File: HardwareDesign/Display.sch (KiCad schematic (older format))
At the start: 30 parts, among them J601 Conn_01x12, U601 Upduino_3.0, U602 IDT7201, U603 74LVC245, U604 74LVC245

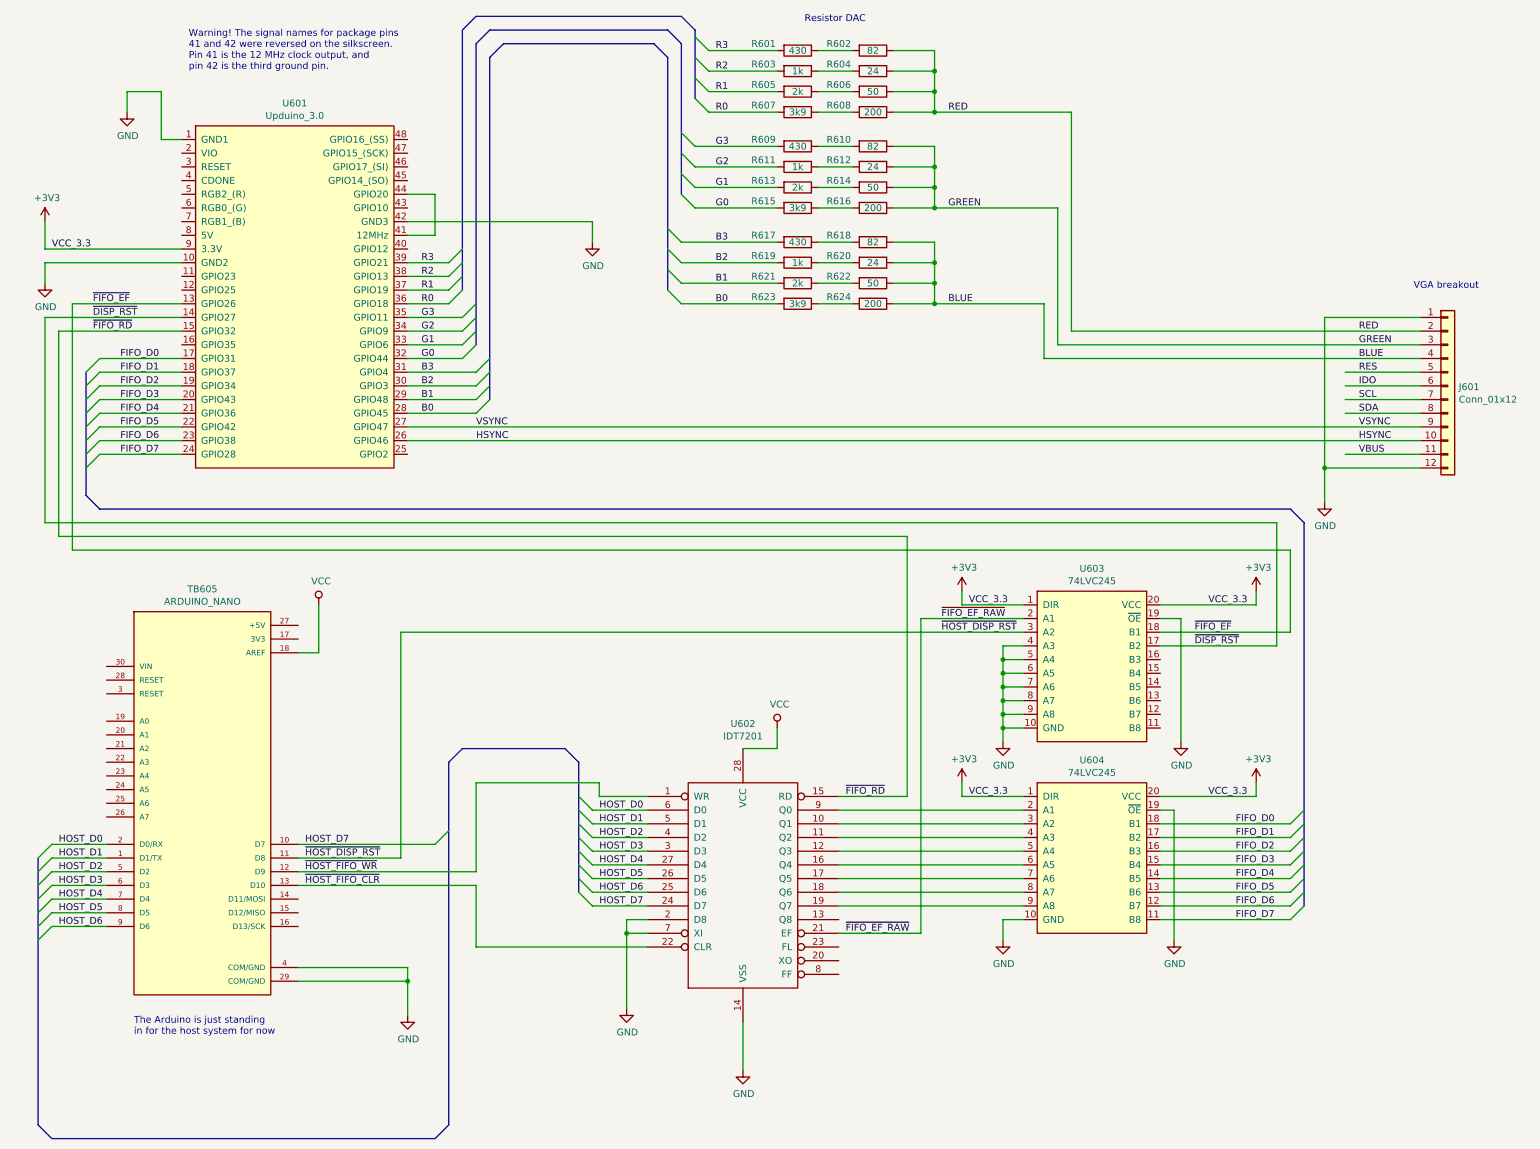
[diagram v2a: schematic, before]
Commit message: more detailed planning for display controller host interface
Enumerated all of the signals in a spreadsheet, making
it explicit which ones require 5V to 3.3V level conversion.

Renamed signals so that there is a more consistent naming
scheme.
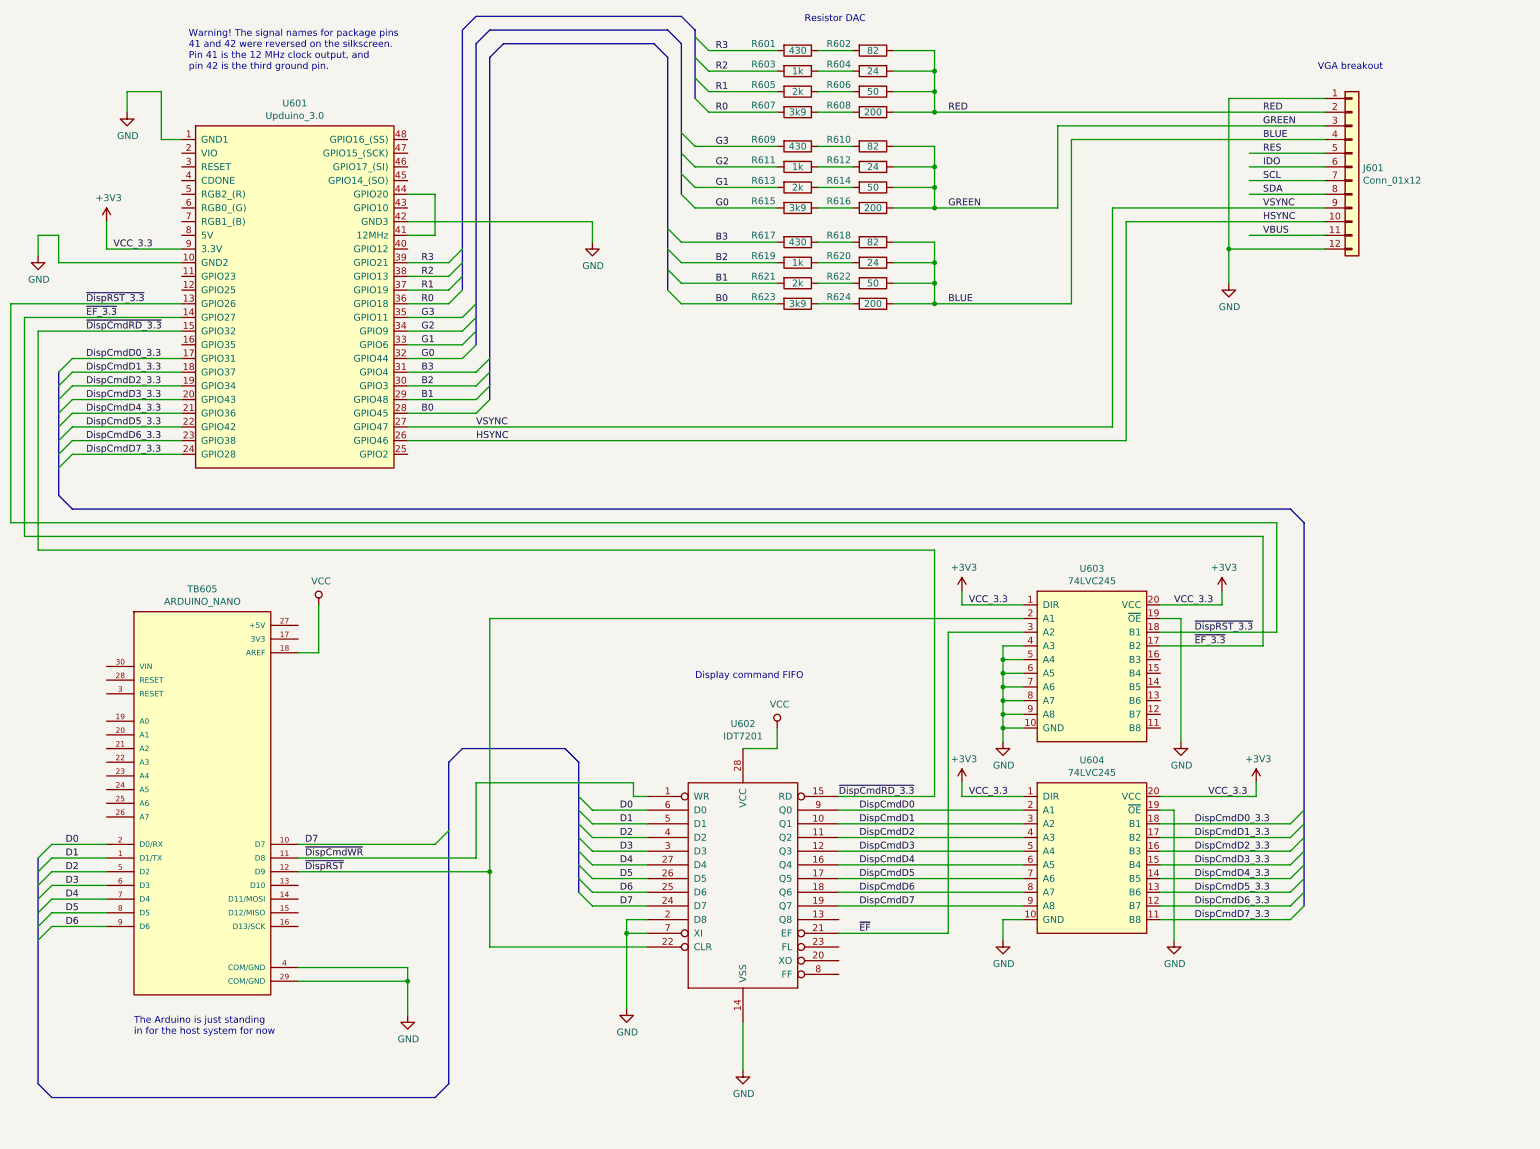
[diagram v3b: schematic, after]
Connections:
- net DispCmdD1: now reaches U602.10 (Q1), U604.3 (A2)
- net DispCmdD2: now reaches U602.11 (Q2), U604.4 (A3)
- net DispCmdD3: now reaches U602.12 (Q3), U604.5 (A4)
- net DispCmdD4: now reaches U602.16 (Q4), U604.6 (A5)
- net DispCmdD5: now reaches U602.17 (Q5), U604.7 (A6)
- net DispCmdD6: now reaches U602.18 (Q6), U604.8 (A7)
- net DispCmdD7: now reaches U602.19 (Q7), U604.9 (A8)
- net DispCmdD0: now reaches U602.9 (Q0), U604.2 (A1)
- net FIFO_D0 renamed DispCmdD0_3.3
- net FIFO_D1 renamed DispCmdD1_3.3
- net FIFO_D2 renamed DispCmdD2_3.3
- net FIFO_D3 renamed DispCmdD3_3.3
- net FIFO_D4 renamed DispCmdD4_3.3
- net FIFO_D5 renamed DispCmdD5_3.3
- net FIFO_D6 renamed DispCmdD6_3.3
- net FIFO_D7 renamed DispCmdD7_3.3
- net HOST_D0 renamed D0
- net HOST_D1 renamed D1
- net HOST_D2 renamed D2
- net HOST_D3 renamed D3
- net HOST_D4 renamed D4
- net HOST_D5 renamed D5
- net HOST_D6 renamed D6
- net HOST_D7 renamed D7
- net ~DISP_RST~ renamed ~EF_3.3~
- net ~FIFO_EF_RAW~ renamed ~DispRST~
- net ~DispRST~: now also TB605.12 (D9), U602.22 (CLR); no longer U602.21 (EF)
- net ~FIFO_EF~ renamed ~DispRST_3.3~
- net ~FIFO_RD~ renamed ~DispCmdRD_3.3~
- net ~HOST_DISP_RST~ renamed ~DispCmdWR~
- net ~DispCmdWR~: now also U602.1 (WR); no longer U603.3 (A2)
- net ~HOST_FIFO_CLR~: no longer names the net of TB605.13 (D10)
- net ~HOST_FIFO_CLR~: no longer U602.22 (CLR)
- removed net ~HOST_FIFO_WR~: TB605.12 (D9), U602.1 (WR)
- new net ~EF~: U602.21 (EF), U603.3 (A2)
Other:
- note added: "Display command FIFO"
- moved on the sheet: J601

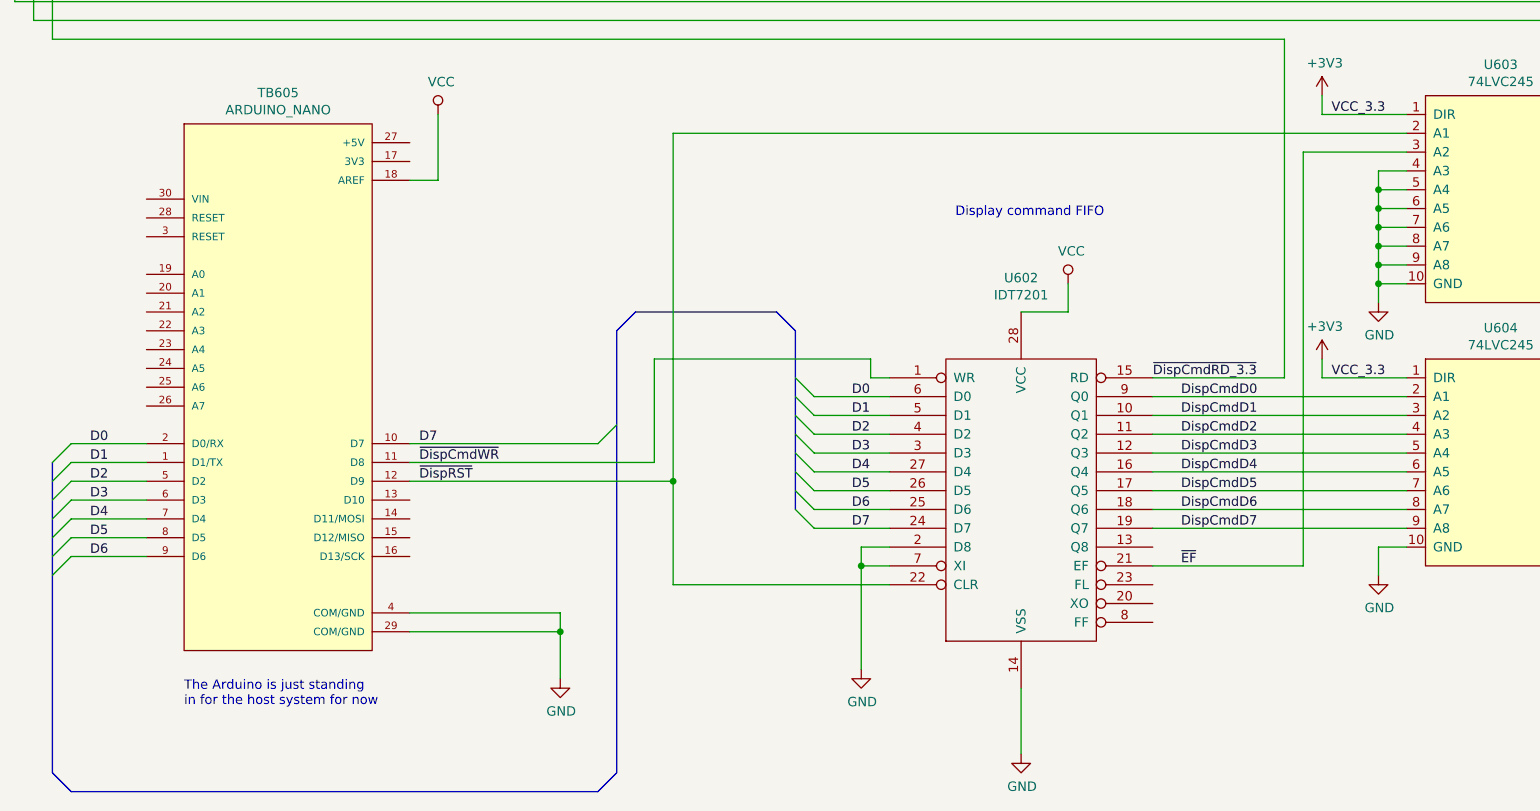
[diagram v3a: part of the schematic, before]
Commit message: added pull-up resistors to data inputs of U604
This ensures that the voltages are at a valid logic
level even when the FIFO is not driving data on its
outputs.

This should also be useful if we add a second FIFO
(e.g., to split command and data streams.)
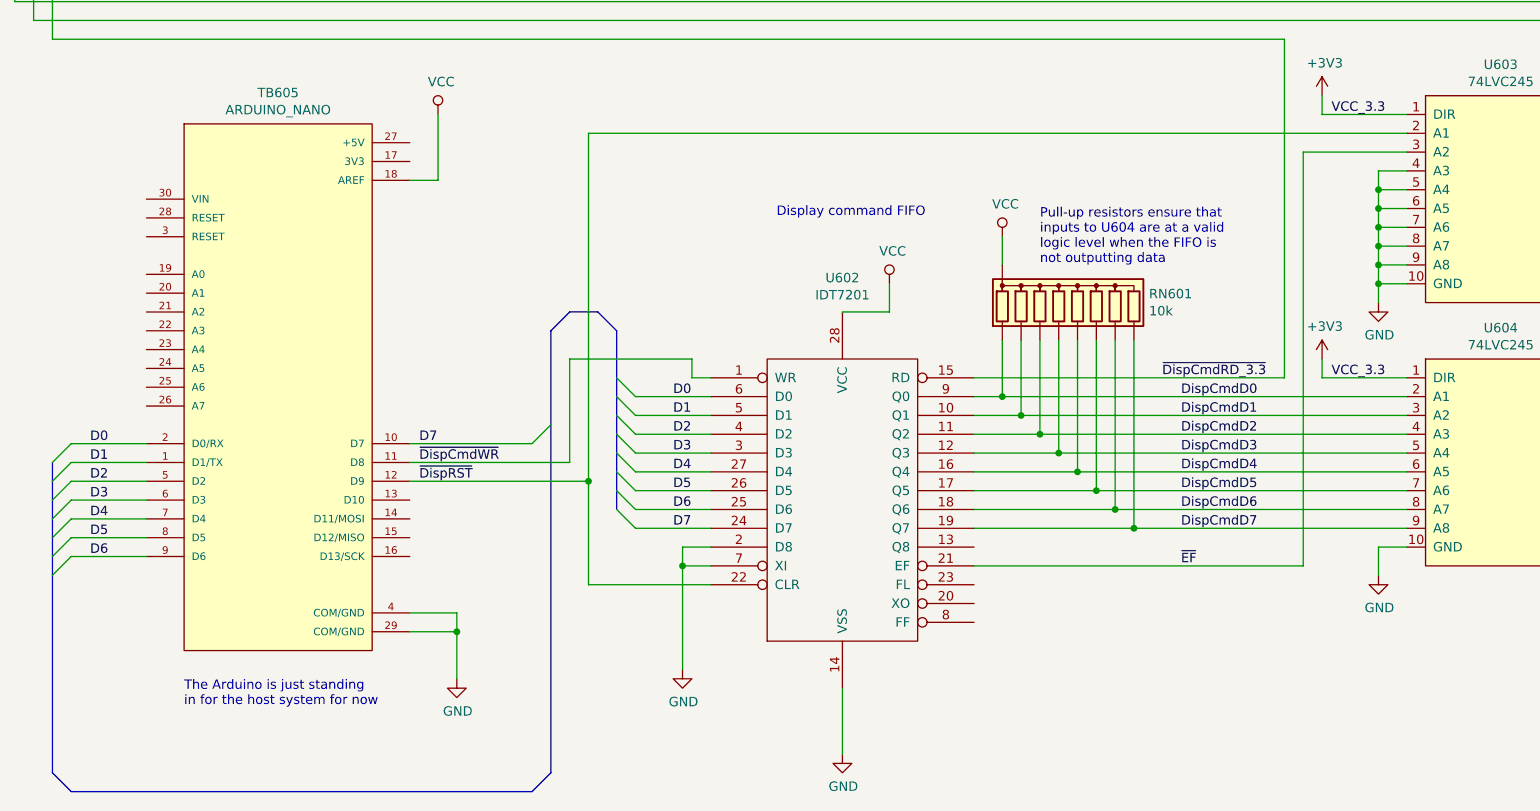
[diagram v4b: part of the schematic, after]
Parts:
- added RN601: 10k, Resistors_THT:R_Array_SIP9, symbol device:R_Network08
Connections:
- net DispCmdD0: now also RN601.2 (R1)
- net DispCmdD1: now also RN601.3 (R2)
- net DispCmdD2: now also RN601.4 (R3)
- net DispCmdD3: now also RN601.5 (R4)
- net DispCmdD4: now also RN601.6 (R5)
- net DispCmdD5: now also RN601.7 (R6)
- net DispCmdD6: now also RN601.8 (R7)
- net DispCmdD7: now also RN601.9 (R8)
- net VCC: now also RN601.1 (common)
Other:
- note added: "Pull-up resistors ensure that\ninputs to U604 are at a valid\nlogic level when the FIFO is\nnot outputting data"
- moved on the sheet: U602

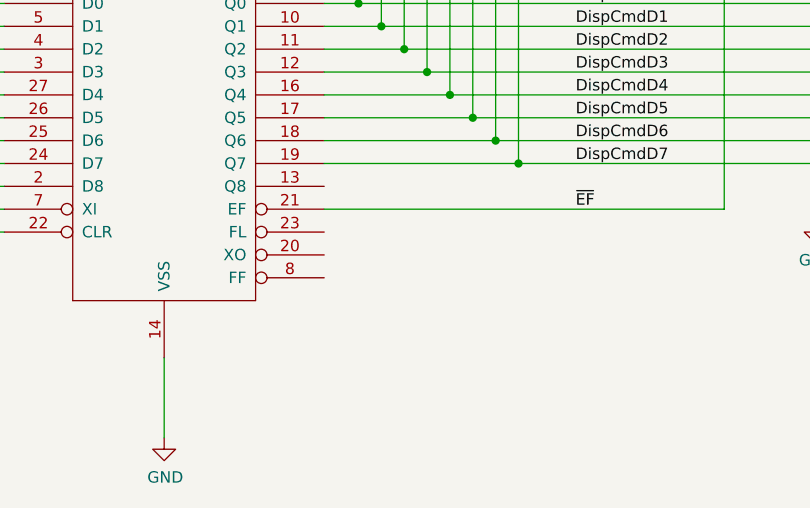
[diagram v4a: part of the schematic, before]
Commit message: tie FIFO -FL input to VCC
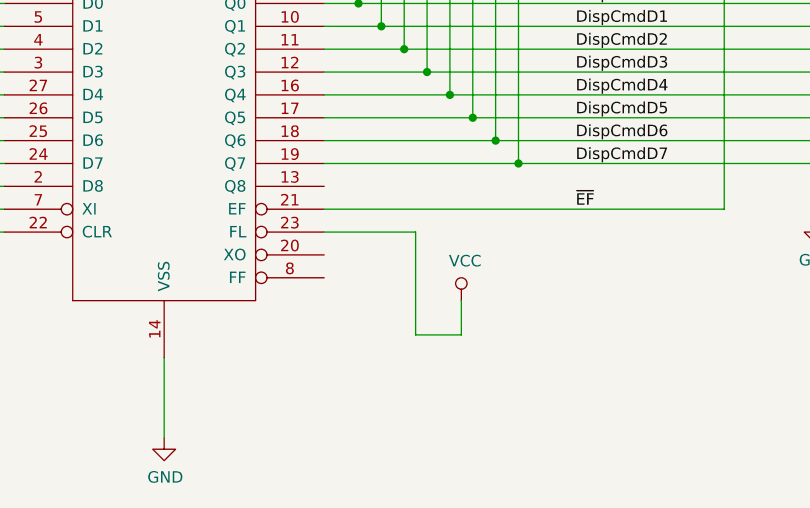
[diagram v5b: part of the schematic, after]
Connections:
- net VCC: now also U602.23 (FL)
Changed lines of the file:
@@
 Wire Wire Line
 	6500 6100 6500 7100
+Connection ~ 6500 7100
+Wire Wire Line
+	6500 7100 5650 7100
+Text Notes 6000 5700 0    50   ~ 0
+Pull-up resistors ensure that\ninputs to U604 are at a valid\nlogic level when the FIFO is\nnot outputting data
+Wire Wire Line
+	5650 7400 6050 7400
+Wire Wire Line
+	6050 7400 6050 7850
+Wire Wire Line
+	6050 7850 6250 7850
+Wire Wire Line
+	6250 7850 6250 7700
 Wire Bus Line
 	3400 6050 3400 8400
@@
 Wire Bus Line
 	900  3200 900  4100
-Connection ~ 6500 7100
-Wire Wire Line
-	6500 7100 5650 7100
-Text Notes 6000 5700 0    50   ~ 0
-Pull-up resistors ensure that\ninputs to U604 are at a valid\nlogic level when the FIFO is\nnot outputting data
+$Comp
+L power:VCC #PWR?
+U 1 1 61D694BA
+P 6250 7700
+F 0 "#PWR?" H 6250 7550 50  0001 C CNN
+F 1 "VCC" H 6267 7873 50  0000 C CNN
+F 2 "" H 6250 7700 50  0001 C CNN
+F 3 "" H 6250 7700 50  0001 C CNN
+	1    6250 7700
+	1    0    0    -1
+$EndComp
 $EndSCHEMATC
